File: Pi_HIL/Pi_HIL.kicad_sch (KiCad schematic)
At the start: 41 parts, among them J1 Raspberry_Pi_2_3, J2 Conn_01x04_Male, J3 Conn_01x04_Male, J4 Conn_01x02_Male, J5 Conn_01x02_Male, J6 Conn_01x03, Q1 MMBT3904, U1 B0505LS-1WR3, U2 ADuM1250ARZ, U3 AMS1117-3.3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

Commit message: Updated Layout + Schematic
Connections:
- net GND: no longer C11.2, C12.2, C6.2, C9.2
- net GND1: now also C11.2, C12.2, C6.2, C9.2
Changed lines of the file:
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@@
 	)
 	(symbol
-		(lib_id "power:GND")
-		(at 227.33 200.66 0)
+		(lib_id "power:GND1")
+		(at 240.03 146.05 0)
 		(unit 1)
 		(exclude_from_sim no)
@@
 		(dnp no)
 		(fields_autoplaced yes)
-		(property "Reference" "#PWR012"
-			(at 227.33 207.01 0)
+		(property "Reference" "#PWR031"
+			(at 240.03 152.4 0)
 			(effects
 				(font
@@
 			)
 		)
-		(property "Value" "GND"
-			(at 227.33 205.74 0)
+		(property "Value" "GND1"
+			(at 240.03 151.13 0)
 			(effects
 				(font
@@
 		)
 		(property "Footprint" ""
-			(at 227.33 200.66 0)
+			(at 240.03 146.05 0)
 			(effects
 				(font
@@
 		)
 		(property "Datasheet" ""
-			(at 227.33 200.66 0)
+			(at 240.03 146.05 0)
 			(effects
 				(font
@@
 		)
 		(property "Description" ""
-			(at 227.33 200.66 0)
+			(at 240.03 146.05 0)
 			(effects
 				(font
@@
 			(project "Pi_HIL"
 				(path "/a3e06eb5-9458-4707-b309-05c4a5721e73"
-					(reference "#PWR012")
+					(reference "#PWR031")
 					(unit 1)
 				)
@@
 	)
 	(symbol
-		(lib_id "power:GND")
-		(at 223.52 260.35 0)
-		(unit 1)
-		(exclude_from_sim no)
-		(in_bom yes)
-		(on_board yes)
-		(dnp no)
-		(fields_autoplaced yes)
-		(property "Reference" "#PWR021"
-			(at 223.52 266.7 0)
-			(effects
-				(font
-					(size 1.27 1.27)
-				)
-				(hide yes)
-			)
-		)
-		(property "Value" "GND"
-			(at 223.52 265.43 0)
-			(effects
-				(font
-					(size 1.27 1.27)
-				)
-			)
-		)
-		(property "Footprint" ""
-			(at 223.52 260.35 0)
-			(effects
-				(font
-					(size 1.27 1.27)
-				)
-				(hide yes)
-			)
-		)
-		(property "Datasheet" ""
-			(at 223.52 260.35 0)
-			(effects
-				(font
-					(size 1.27 1.27)
-				)
-				(hide yes)
-			)
-		)
-		(property "Description" ""
-			(at 223.52 260.35 0)
-			(effects
-				(font
-					(size 1.27 1.27)
-				)
-				(hide yes)
-			)
-		)
-		(pin "1"
-		)
-		(instances
-			(project "Pi_HIL"
-				(path "/a3e06eb5-9458-4707-b309-05c4a5721e73"
-					(reference "#PWR021")
-					(unit 1)
-				)
-			)
-		)
-	)
-	(symbol
 		(lib_id "Device:C")
 		(at 142.24 92.71 0)
@@
 	(symbol
 		(lib_id "power:GND")
-		(at 240.03 146.05 0)
-		(unit 1)
-		(exclude_from_sim no)
-		(in_bom yes)
-		(on_board yes)
-		(dnp no)
-		(fields_autoplaced yes)
-		(property "Reference" "#PWR031"
-			(at 240.03 152.4 0)
-			(effects
-				(font
-					(size 1.27 1.27)
-				)
-				(hide yes)
-			)
-		)
-		(property "Value" "GND"
-			(at 240.03 151.13 0)
-			(effects
-				(font
-					(size 1.27 1.27)
-				)
-			)
-		)
-		(property "Footprint" ""
-			(at 240.03 146.05 0)
-			(effects
-				(font
-					(size 1.27 1.27)
-				)
-				(hide yes)
-			)
-		)
-		(property "Datasheet" ""
-			(at 240.03 146.05 0)
-			(effects
-				(font
-					(size 1.27 1.27)
-				)
-				(hide yes)
-			)
-		)
-		(property "Description" ""
-			(at 240.03 146.05 0)
-			(effects
-				(font
-					(size 1.27 1.27)
-				)
-				(hide yes)
-			)
-		)
-		(pin "1"
-		)
-		(instances
-			(project "Pi_HIL"
-				(path "/a3e06eb5-9458-4707-b309-05c4a5721e73"
-					(reference "#PWR031")
-					(unit 1)
-				)
-			)
-		)
-	)
-	(symbol
-		(lib_id "power:GND")
 		(at 173.99 110.49 0)
 		(unit 1)
@@
 	(symbol
 		(lib_id "power:GND1")
+		(at 223.52 260.35 0)
+		(unit 1)
+		(exclude_from_sim no)
+		(in_bom yes)
+		(on_board yes)
+		(dnp no)
+		(fields_autoplaced yes)
+		(property "Reference" "#PWR021"
+			(at 223.52 266.7 0)
+			(effects
+				(font
+					(size 1.27 1.27)
+				)
+				(hide yes)
+			)
+		)
+		(property "Value" "GND1"
+			(at 223.52 265.43 0)
+			(effects
+				(font
+					(size 1.27 1.27)
+				)
+			)
+		)
+		(property "Footprint" ""
+			(at 223.52 260.35 0)
+			(effects
+				(font
+					(size 1.27 1.27)
+				)
+				(hide yes)
+			)
+		)
+		(property "Datasheet" ""
+			(at 223.52 260.35 0)
+			(effects
+				(font
+					(size 1.27 1.27)
+				)
+				(hide yes)
+			)
+		)
+		(property "Description" ""
+			(at 223.52 260.35 0)
+			(effects
+				(font
+					(size 1.27 1.27)
+				)
+				(hide yes)
+			)
+		)
+		(pin "1"
+		)
+		(instances
+			(project "Pi_HIL"
+				(path "/a3e06eb5-9458-4707-b309-05c4a5721e73"
+					(reference "#PWR021")
+					(unit 1)
+				)
+			)
+		)
+	)
+	(symbol
+		(lib_id "power:GND1")
 		(at 217.17 147.32 0)
 		(unit 1)
@@
 	)
 	(symbol
+		(lib_id "power:GND1")
+		(at 261.62 99.06 0)
+		(unit 1)
+		(exclude_from_sim no)
+		(in_bom yes)
+		(on_board yes)
+		(dnp no)
+		(fields_autoplaced yes)
+		(property "Reference" "#PWR032"
+			(at 261.62 105.41 0)
+			(effects
+				(font
+					(size 1.27 1.27)
+				)
+				(hide yes)
+			)
+		)
+		(property "Value" "GND1"
+			(at 261.62 104.14 0)
+			(effects
+				(font
+					(size 1.27 1.27)
+				)
+			)
+		)
+		(property "Footprint" ""
+			(at 261.62 99.06 0)
+			(effects
+				(font
+					(size 1.27 1.27)
+				)
+				(hide yes)
+			)
+		)
+		(property "Datasheet" ""
+			(at 261.62 99.06 0)
+			(effects
+				(font
+					(size 1.27 1.27)
+				)
+				(hide yes)
+			)
+		)
+		(property "Description" ""
+			(at 261.62 99.06 0)
+			(effects
+				(font
+					(size 1.27 1.27)
+				)
+				(hide yes)
+			)
+		)
+		(pin "1"
+		)
+		(instances
+			(project "Pi_HIL"
+				(path "/a3e06eb5-9458-4707-b309-05c4a5721e73"
+					(reference "#PWR032")
+					(unit 1)
+				)
+			)
+		)
+	)
+	(symbol
 		(lib_id "power:GND")
 		(at 157.48 147.32 0)
@@
 	)
 	(symbol
-		(lib_id "power:GND")
-		(at 261.62 99.06 0)
-		(unit 1)
-		(exclude_from_sim no)
-		(in_bom yes)
-		(on_board yes)
-		(dnp no)
-		(fields_autoplaced yes)
-		(property "Reference" "#PWR032"
-			(at 261.62 105.41 0)
-			(effects
-				(font
-					(size 1.27 1.27)
-				)
-				(hide yes)
-			)
-		)
-		(property "Value" "GND"
-			(at 261.62 104.14 0)
-			(effects
-				(font
-					(size 1.27 1.27)
-				)
-			)
-		)
-		(property "Footprint" ""
-			(at 261.62 99.06 0)
-			(effects
-				(font
-					(size 1.27 1.27)
-				)
-				(hide yes)
-			)
-		)
-		(property "Datasheet" ""
-			(at 261.62 99.06 0)
-			(effects
-				(font
-					(size 1.27 1.27)
-				)
-				(hide yes)
-			)
-		)
-		(property "Description" ""
-			(at 261.62 99.06 0)
-			(effects
-				(font
-					(size 1.27 1.27)
-				)
-				(hide yes)
-			)
-		)
-		(pin "1"
-		)
-		(instances
-			(project "Pi_HIL"
-				(path "/a3e06eb5-9458-4707-b309-05c4a5721e73"
-					(reference "#PWR032")
-					(unit 1)
-				)
-			)
-		)
-	)
-	(symbol
 		(lib_id "Device:R")
 		(at 67.31 116.84 90)
@@
 					(unit 1)
 				)
+			)
+		)
+	)
+	(symbol
+		(lib_id "power:GND1")
+		(at 227.33 200.66 0)
+		(unit 1)
+		(exclude_from_sim no)
+		(in_bom yes)
+		(on_board yes)
+		(dnp no)
+		(fields_autoplaced yes)
+		(property "Reference" "#PWR012"
+			(at 227.33 207.01 0)
+			(effects
+				(font
+					(size 1.27 1.27)
+				)
+				(hide yes)
+			)
+		)
+		(property "Value" "GND1"
+			(at 227.33 205.74 0)
+			(effects
+				(font
+					(size 1.27 1.27)
+				)
+			)
+		)
+		(property "Footprint" ""
+			(at 227.33 200.66 0)
+			(effects
+				(font
+					(size 1.27 1.27)
+				)
+				(hide yes)
+			)
+		)
+		(property "Datasheet" ""
+			(at 227.33 200.66 0)
+			(effects
+				(font
+					(size 1.27 1.27)
+				)
+				(hide yes)
+			)
+		)
+		(property "Description" ""
+			(at 227.33 200.66 0)
+			(effects
+				(font
+					(size 1.27 1.27)
+				)
+				(hide yes)
+			)
+		)
+		(pin "1"
+		)
+		(instances
+			(project "Pi_HIL"
+				(path "/a3e06eb5-9458-4707-b309-05c4a5721e73"
+					(reference "#PWR012")
+					(unit 1)
+				)

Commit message: Updated Layout, added UART + I2C headers
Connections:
- net ADC_AIN2: now also J3.4 (Pin_4); no longer J3.3 (Pin_3)
- net ADC_AIN3: now also J3.3 (Pin_3); no longer J3.4 (Pin_4)
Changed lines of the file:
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@@
 		)
 	)
-	(label "ADC_AIN2"
+	(label "ADC_AIN3"
 		(at 349.25 186.69 0)
 		(fields_autoplaced yes)
@@
 		)
 	)
-	(label "ADC_AIN3"
+	(label "ADC_AIN2"
 		(at 349.25 189.23 0)
 		(fields_autoplaced yes)

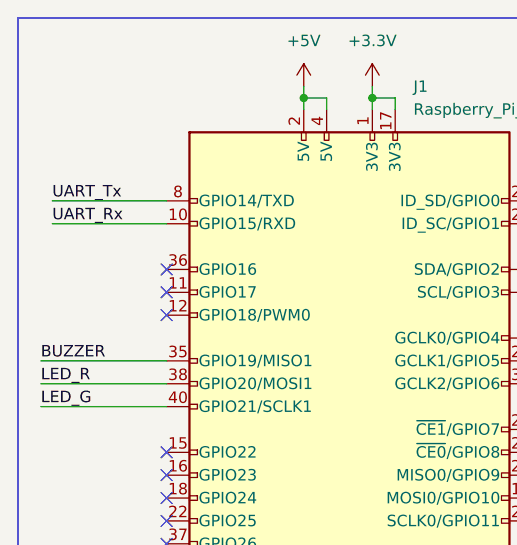
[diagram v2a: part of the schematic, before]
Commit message: Connected LED D3 to GPIO 16
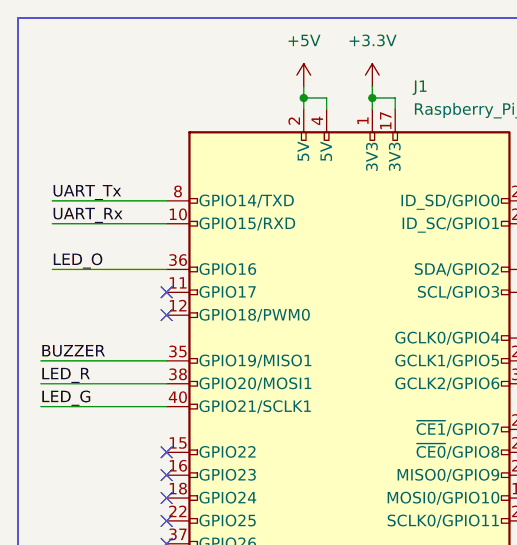
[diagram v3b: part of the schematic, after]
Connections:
- net LED_O: now also J1.36 (GPIO16)
- no-connect marks 21 -> 20
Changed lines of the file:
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@@
-	)
-	(no_connect
-		(at 30.48 41.91)
 	)
 	(no_connect
@@
 		(pts
 			(xy 157.48 135.89) (xy 181.61 135.89)
+		)
+		(stroke
+			(width 0)
+			(type default)
+		)
+	)
+	(wire
+		(pts
+			(xy 17.78 41.91) (xy 30.48 41.91)
 		)
 		(stroke
@@
 		(fields_autoplaced yes)
 		(effects
+			(font
+				(size 1.27 1.27)
+			)
+			(justify left bottom)
+		)
+	)
+	(label "LED_O"
+		(at 17.78 41.91 0)
+		(fields_autoplaced yes)
+		(effects
